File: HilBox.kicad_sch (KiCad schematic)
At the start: 5 parts, among them SW1 SW_DIP_x06

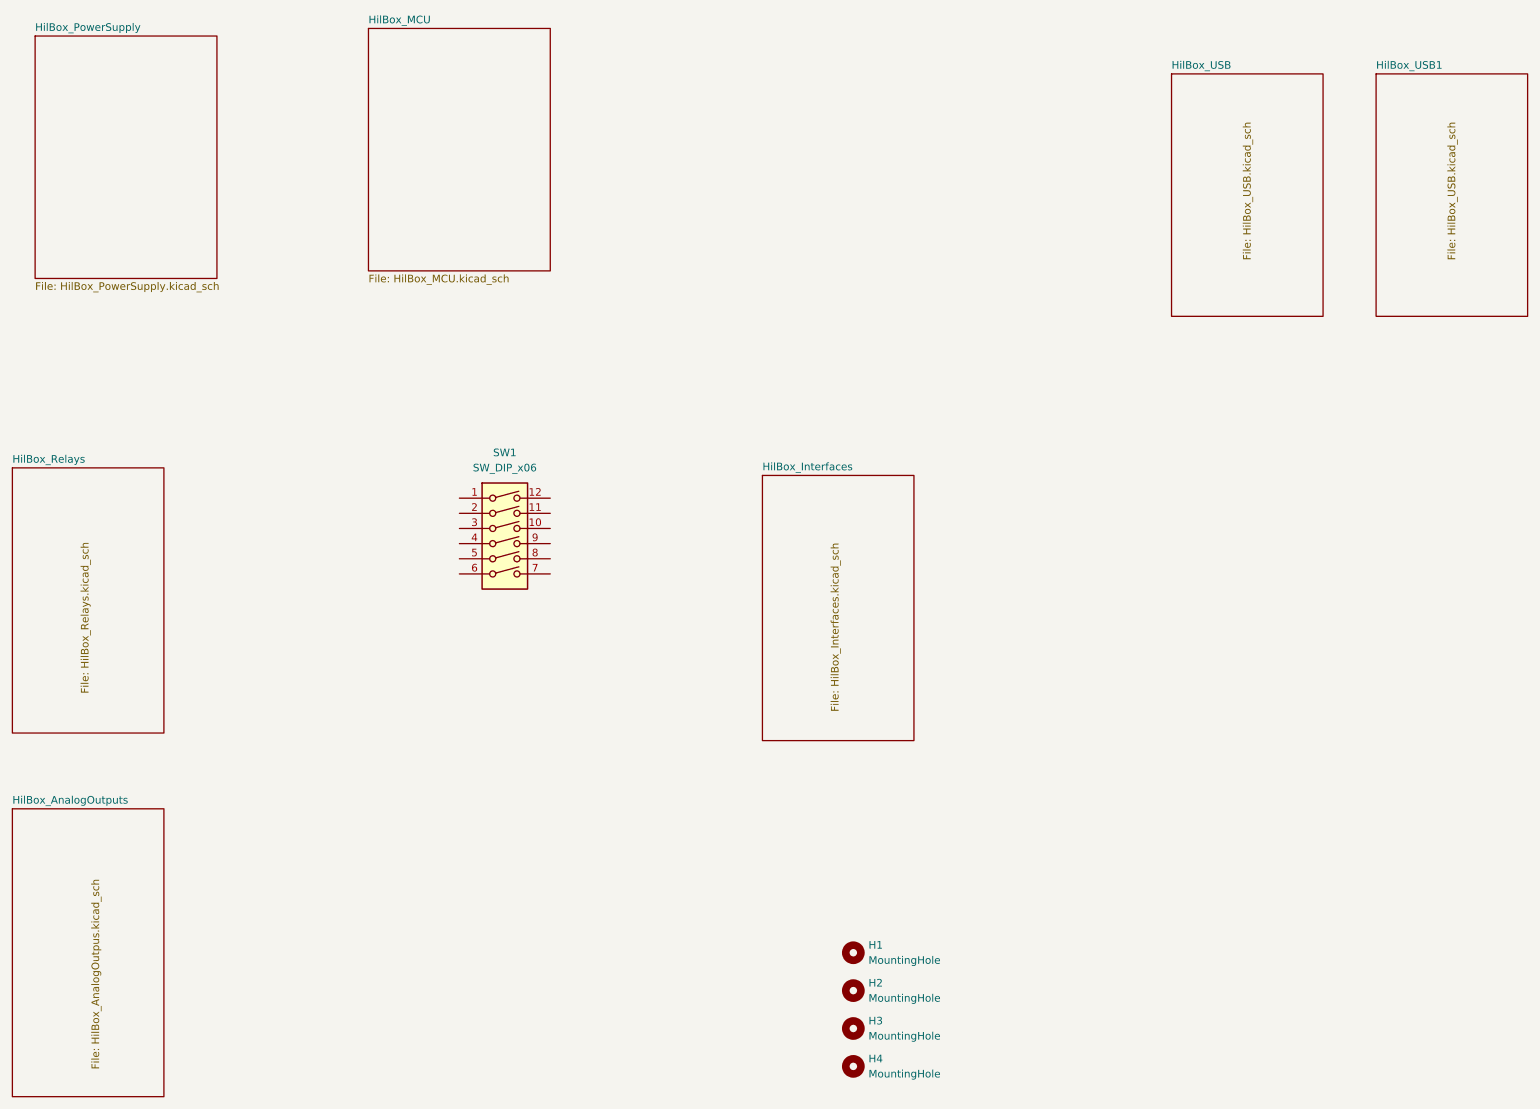
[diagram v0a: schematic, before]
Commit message: Modification in half of target
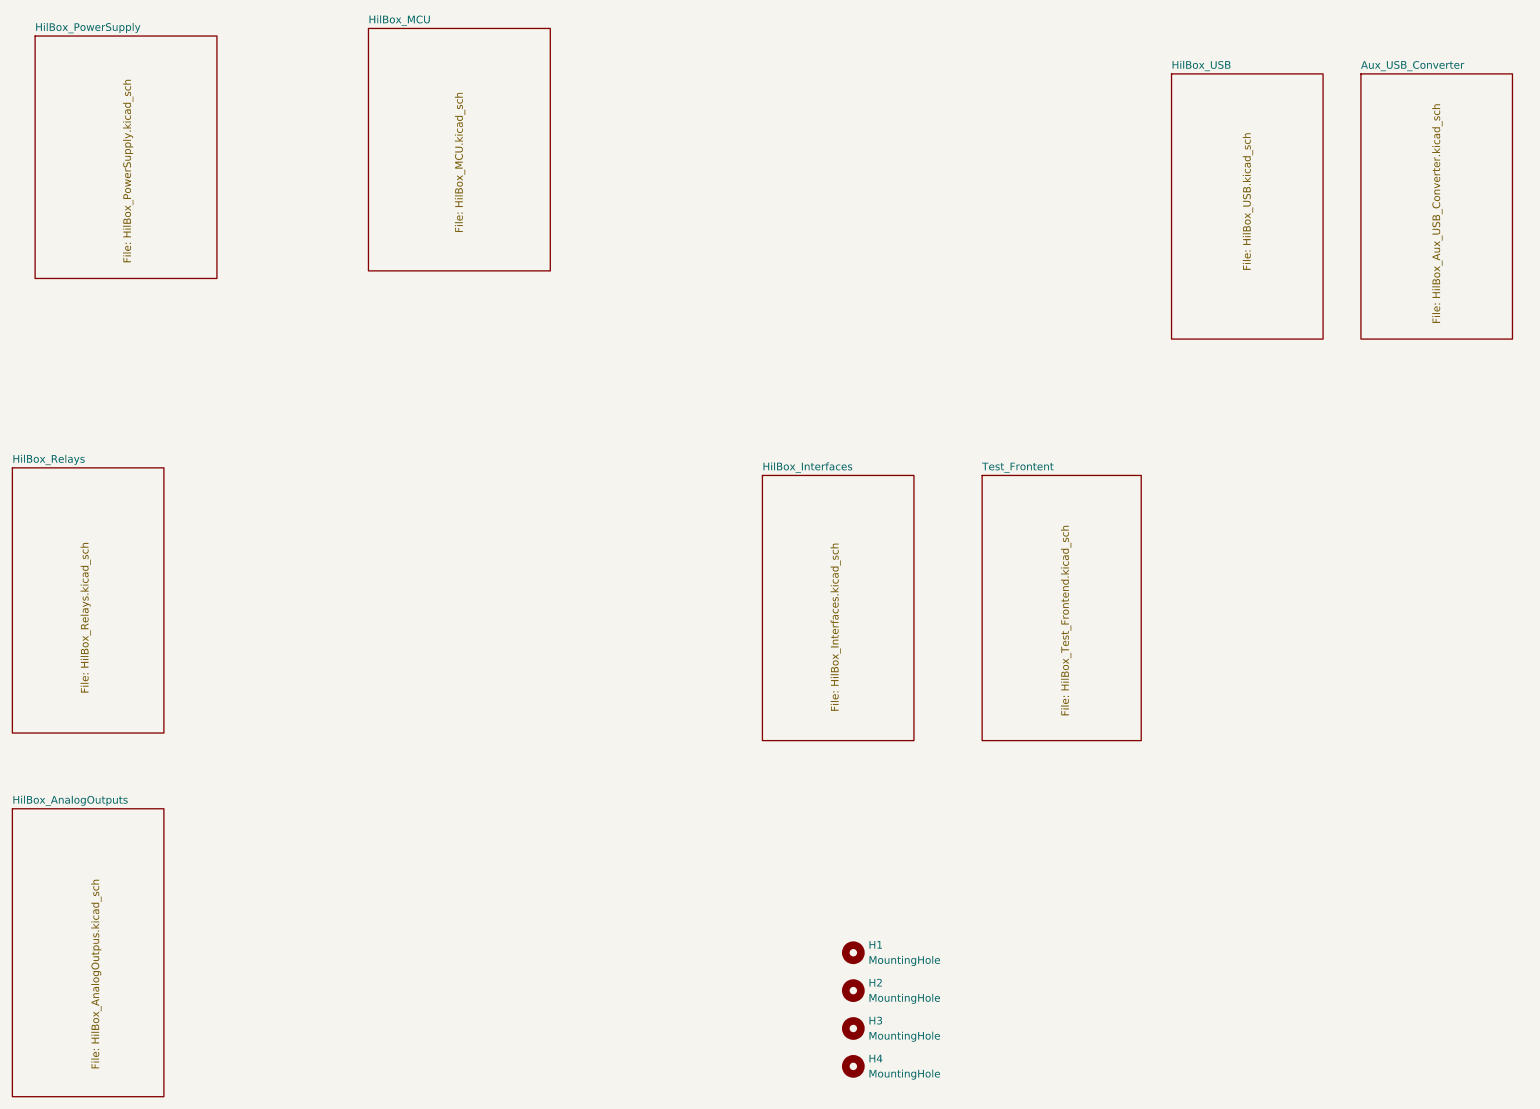
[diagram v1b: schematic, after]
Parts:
- removed SW1: SW_DIP_x06, symbol Switch:SW_DIP_x06
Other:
- removed sheet HilBox_USB1
- added sheet Aux_USB_Converter (HilBox_Aux_USB_Converter.kicad_sch)
- added sheet Test_Frontent (HilBox_Test_Frontend.kicad_sch)
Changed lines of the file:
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@@
-	)
-	(symbol
-		(lib_id "Switch:SW_DIP_x06")
-		(at 99.06 102.87 0)
-		(unit 1)
-		(exclude_from_sim no)
-		(in_bom yes)
-		(on_board yes)
-		(dnp no)
-		(fields_autoplaced yes)
-		(property "Reference" "SW1"
-			(at 99.06 87.63 0)
-			(effects
-				(font
-					(size 1.27 1.27)
-				)
-			)
-		)
-		(property "Value" "SW_DIP_x06"
-			(at 99.06 90.17 0)
-			(effects
-				(font
-					(size 1.27 1.27)
-				)
-			)
-		)
-		(property "Footprint" ""
-			(at 99.06 102.87 0)
-			(effects
-				(font
-					(size 1.27 1.27)
-				)
-				(hide yes)
-			)
-		)
-		(property "Datasheet" "~"
-			(at 99.06 102.87 0)
-			(effects
-				(font
-					(size 1.27 1.27)
-				)
-				(hide yes)
-			)
-		)
-		(property "Description" "6x DIP Switch, Single Pole Single Throw (SPST) switch, small symbol"
-			(at 99.06 102.87 0)
-			(effects
-				(font
-					(size 1.27 1.27)
-				)
-				(hide yes)
-			)
-		)
-		(pin "3"
-		)
-		(pin "5"
-		)
-		(pin "1"
-		)
-		(pin "2"
-		)
-		(pin "4"
-		)
-		(pin "11"
-		)
-		(pin "10"
-		)
-		(pin "6"
-		)
-		(pin "12"
-		)
-		(pin "8"
-		)
-		(pin "9"
-		)
-		(pin "7"
-		)
-		(instances
-			(project ""
-				(path "/c950b3bb-3e52-4d0d-8bbf-240895efa80b"
-					(reference "SW1")
-					(unit 1)
-				)
-			)
-		)
 	)
 	(symbol
@@
 		(on_board yes)
 		(dnp no)
-		(fields_autoplaced yes)
 		(stroke
 			(width 0.1524)
@@
 		)
 		(property "Sheetfile" "HilBox_PowerSupply.kicad_sch"
-			(at 20.32 59.0046 0)
+			(at 35.052 55.88 90)
 			(effects
 				(font
@@
 	(sheet
 		(at 210.82 24.13)
-		(size 25.4 40.64)
+		(size 25.4 44.45)
 		(exclude_from_sim no)
 		(in_bom yes)
@@
 		)
 		(property "Sheetfile" "HilBox_USB.kicad_sch"
-			(at 222.758 55.372 90)
+			(at 222.758 57.15 90)
 			(effects
 				(font
@@
 		(on_board yes)
 		(dnp no)
-		(fields_autoplaced yes)
 		(stroke
 			(width 0.1524)
@@
 		)
 		(property "Sheetfile" "HilBox_MCU.kicad_sch"
-			(at 76.2 57.7346 0)
+			(at 90.678 50.8 90)
 			(effects
 				(font
@@
 	)
 	(sheet
-		(at 245.11 24.13)
-		(size 25.4 40.64)
-		(exclude_from_sim no)
-		(in_bom yes)
-		(on_board yes)
-		(dnp no)
-		(stroke
-			(width 0.1524)
-			(type solid)
-		)
-		(fill
-			(color 0 0 0 0.0000)
-		)
-		(property "Sheetname" "HilBox_USB1"
-			(at 245.11 23.4184 0)
-			(effects
-				(font
-					(size 1.27 1.27)
-				)
-				(justify left bottom)
-			)
-		)
-		(property "Sheetfile" "HilBox_USB.kicad_sch"
-			(at 257.048 55.372 90)
-			(effects
-				(font
-					(size 1.27 1.27)
-				)
-				(justify left top)
-			)
-		)
-		(property "Field2" ""
-			(at 245.11 24.13 0)
-			(effects
-				(font
-					(size 1.27 1.27)
-				)
-				(hide yes)
-			)
-		)
-		(instances
-			(project "HilBox"
-				(path "/c950b3bb-3e52-4d0d-8bbf-240895efa80b"
-					(page "5")
+		(at 242.57 24.13)
+		(size 25.4 44.45)
+		(exclude_from_sim no)
+		(in_bom yes)
+		(on_board yes)
+		(dnp no)
+		(stroke
+			(width 0.1524)
+			(type solid)
+		)
+		(fill
+			(color 0 0 0 0.0000)
+		)
+		(property "Sheetname" "Aux_USB_Converter"
+			(at 242.57 23.4184 0)
+			(effects
+				(font
+					(size 1.27 1.27)
+				)
+				(justify left bottom)
+			)
+		)
+		(property "Sheetfile" "HilBox_Aux_USB_Converter.kicad_sch"
+			(at 254.508 66.04 90)
+			(effects
+				(font
+					(size 1.27 1.27)
+				)
+				(justify left top)
+			)
+		)
+		(instances
+			(project "HilBox"
+				(path "/c950b3bb-3e52-4d0d-8bbf-240895efa80b"
+					(page "8")
 				)
 			)
@@
 				)
 			)
+		)
+	)
+	(sheet
+		(at 179.07 91.44)
+		(size 26.67 44.45)
+		(exclude_from_sim no)
+		(in_bom yes)
+		(on_board yes)
+		(dnp no)
+		(stroke
+			(width 0.1524)
+			(type solid)
+		)
+		(fill
+			(color 0 0 0 0.0000)
+		)
+		(property "Sheetname" "Test_Frontent"
+			(at 179.07 90.7284 0)
+			(effects
+				(font
+					(size 1.27 1.27)
+				)
+				(justify left bottom)
+			)
+		)
+		(property "Sheetfile" "HilBox_Test_Frontend.kicad_sch"
+			(at 192.278 131.826 90)
+			(effects
+				(font
+					(size 1.27 1.27)
+				)
+				(justify left top)
+			)
+		)
+		(instances
+			(project "HilBox"
+				(path "/c950b3bb-3e52-4d0d-8bbf-240895efa80b"
+					(page "9")
+				)
+			)

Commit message: Schematic design at finish
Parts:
- added J1: Conn_01x20_Pin, Connectors:Terminal_Block_3_81_20p_Horizontal, symbol Connector:Conn_01x20_Pin
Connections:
- new net CANH: J1.3 (Pin_3)
- new net CANL: J1.4 (Pin_4)
- new net ESP32_RX: J1.7 (Pin_7)
- new net ESP32_TX: J1.8 (Pin_8)
- new net RS485_A: J1.6 (Pin_6)
- new net RS485_B: J1.5 (Pin_5)

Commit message: Layout 90% done
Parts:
- added C22: 100n/50V, Capacitor_SMD:C_0402_1005Metric, symbol Device:C
- added C3, C5: 68p/50V, Capacitor_SMD:C_0402_1005Metric, symbol Device:C
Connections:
- net CANH: now also J1.18 (Pin_18); no longer J1.3 (Pin_3)
- net CANL: now also J1.17 (Pin_17); no longer J1.4 (Pin_4)
- net RS485_A: now also J1.15 (Pin_15); no longer J1.6 (Pin_6)
- net RS485_B: now also J1.16 (Pin_16); no longer J1.5 (Pin_5)
- net GND: now reaches J1.10 (Pin_10)
- net GND: now also J1.12 (Pin_12), J1.19 (Pin_19), C22.2, C3.2, C5.2
- net SM: now reaches J1.11 (Pin_11)
- net AUXUART_RX: now reaches J1.13 (Pin_13)
- net AUXUART_RX: now also C3.1
- net AUXUART_TX: now reaches J1.14 (Pin_14)
- net AUXUART_TX: now also C5.1
- net 24V: now reaches J1.20 (Pin_20)
- net 24V: now also C22.1
- net SR: now reaches J1.9 (Pin_9)
- net ESP32_RX: no longer names the net of J1.7 (Pin_7)
- net ESP32_TX: no longer names the net of J1.8 (Pin_8)

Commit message: Gate finalized! PCB ordered
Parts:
- added H5, H6: MountingHole, MountingHole:MountingHole_2.2mm_M2, symbol Mechanical:MountingHole
- J1: JLC_PN (none) -> C430380
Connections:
- net RLY4_B: now reaches J1.1 (Pin_1)
- net RLY4_A: now reaches J1.2 (Pin_2)
- net RLY3_B: now reaches J1.3 (Pin_3)
- net RLY3_A: now reaches J1.4 (Pin_4)
- net RLY2_B: now reaches J1.5 (Pin_5)
- net RLY2_A: now reaches J1.6 (Pin_6)
- net RLY1_B: now reaches J1.7 (Pin_7)
- net RLY1_A: now reaches J1.8 (Pin_8)
- net 24V renamed Vin
